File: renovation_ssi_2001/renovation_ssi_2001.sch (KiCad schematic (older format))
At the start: 72 parts, among them J1 KLPX-0848A-2-B, J2 DB15_Female, J4 Bus_ISA_8bit, J5 Pins_02x04, J6 Pins_02x03, J7 SID_Socket, Q1 PN2222A, Q2 PN2222A, U1 74LS74, U10 74LS138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

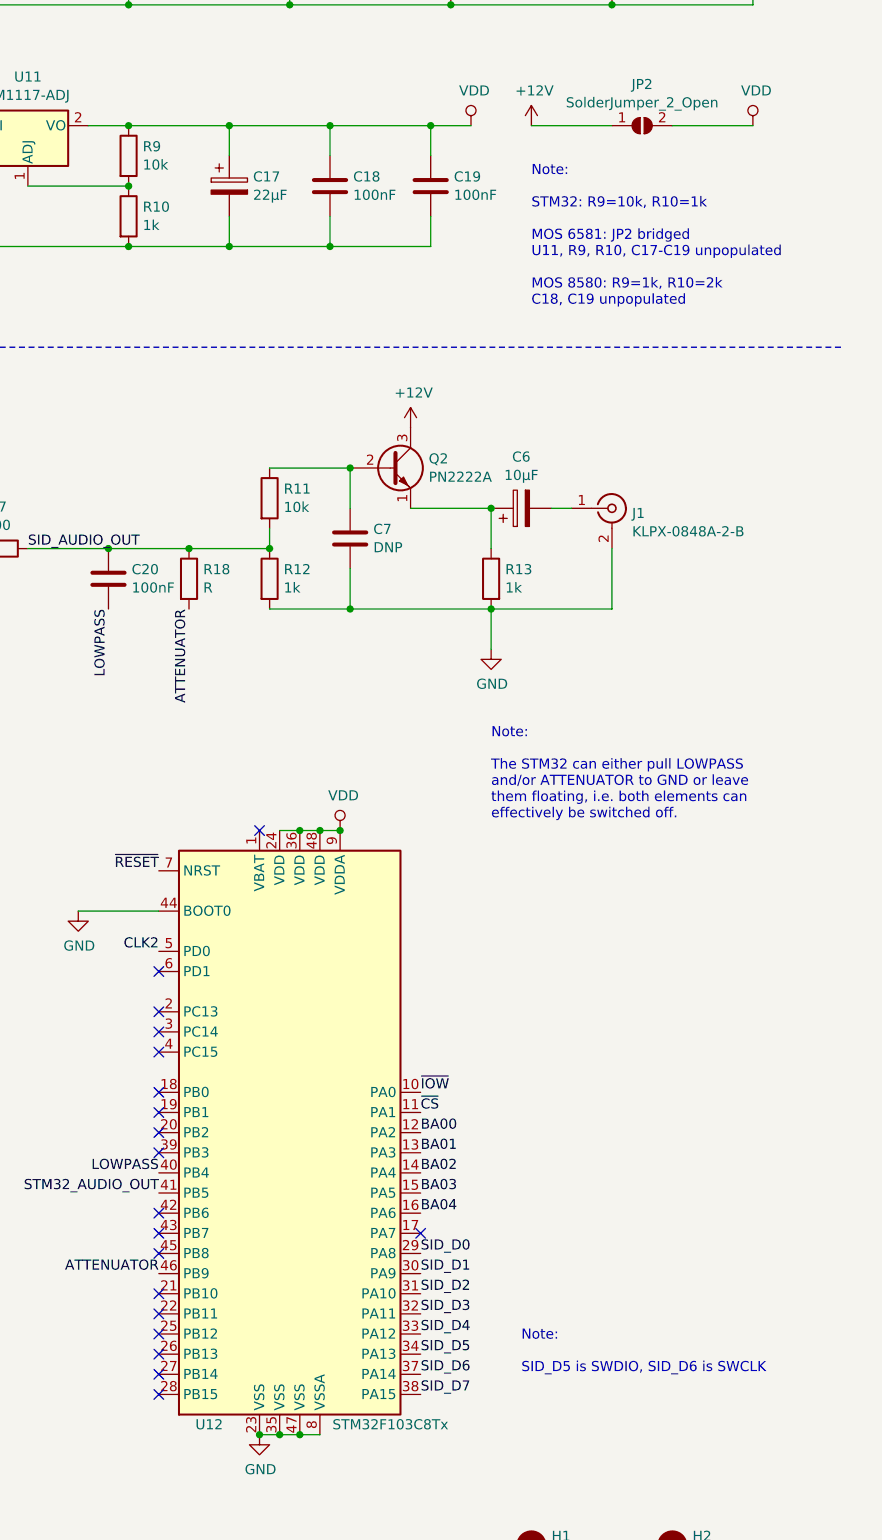
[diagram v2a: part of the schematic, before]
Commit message: correct configuration resistor values for the voltage regulator
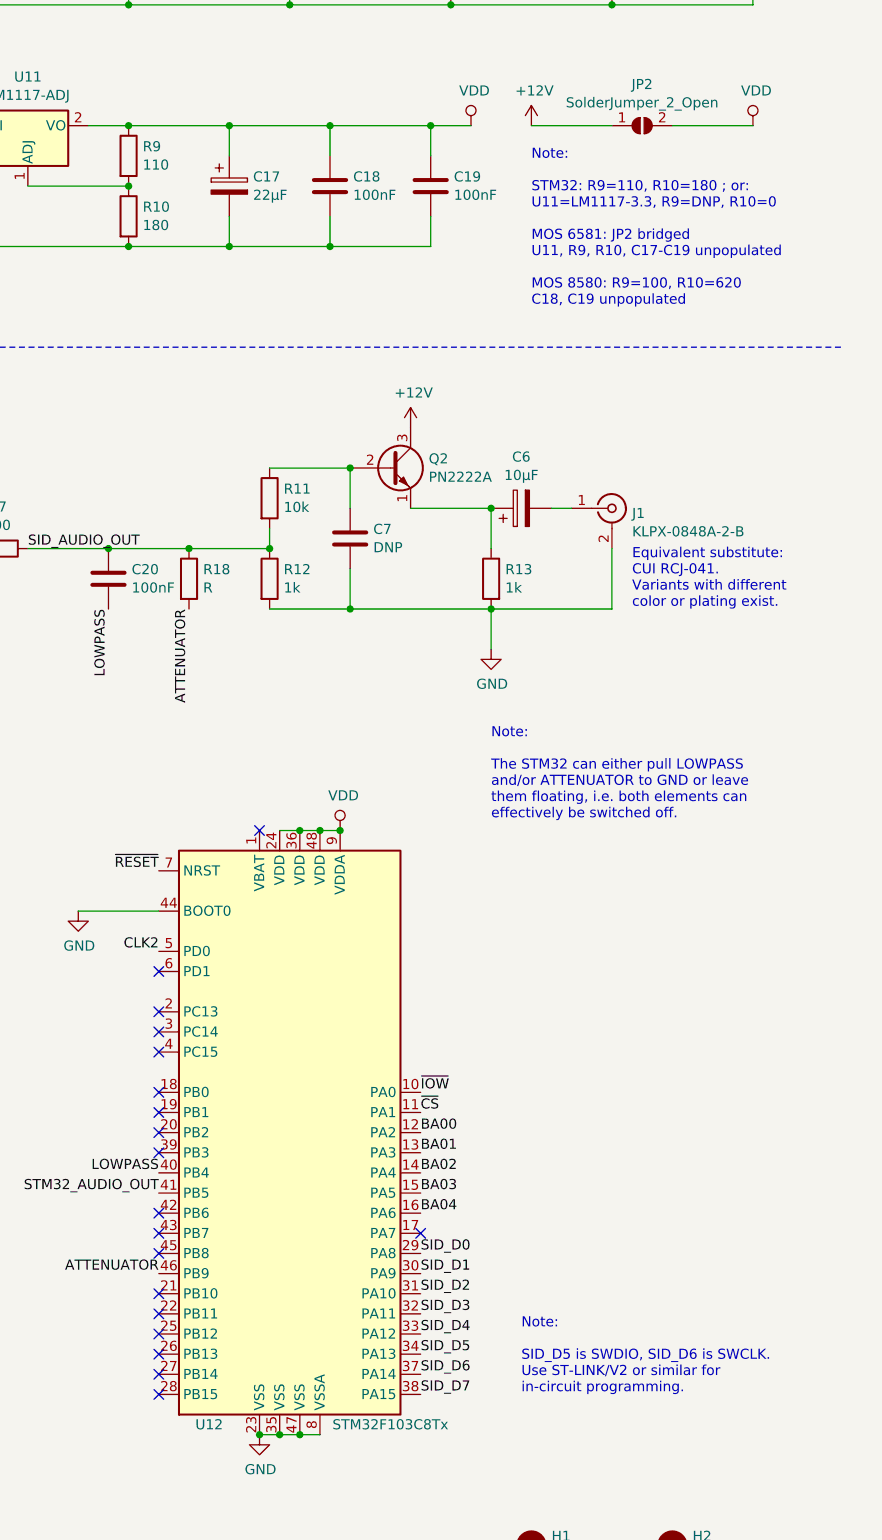
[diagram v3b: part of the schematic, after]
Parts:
- R10: value 1k -> 180
- R9: value 10k -> 110
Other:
- note added: "Equivalent substitute:\nCUI RCJ-041.\nVariants with different\ncolor or plating exist."
- note added: "Note:\n\nSID_D5 is SWDIO, SID_D6 is SWCLK.\nUse ST-LINK/V2 or similar for\nin-circuit programming."
- note added: "Note:\n\nSTM32: R9=110, R10=180 ; or:\nU11=LM1117-3.3, R9=DNP, R10=0\n\nMOS 6581: JP2 bridged\nU11, R9, R10, C17-C19 unpopulated\n\nMOS 8580: R9=100, R10=620\nC18, C19 unpopulated"
- note removed: "Note:\n\nSID_D5 is SWDIO, SID_D6 is SWCLK"
- note removed: "Note:\n\nSTM32: R9=10k, R10=1k\n\nMOS 6581: JP2 bridged\nU11, R9, R10, C17-C19 unpopulated\n\nMOS 8580: R9=1k, R10=2k\nC18, C19 unpopulated"
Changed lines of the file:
@@
 Sheet 1 1
 Title "RENOVATION SSI-2001"
-Date "2020-03-10"
+Date "2020-03-13"
 Rev ""
 Comp "Benedikt Freisen"
@@
 NoConn ~ 12650 7000
 NoConn ~ 13950 7900
-Text Notes 14450 8600 0    50   ~ 0
-Note:\n\nSID_D5 is SWDIO, SID_D6 is SWCLK
 NoConn ~ 12650 7200
 NoConn ~ 12650 7300
@@
 P 12500 2550
 F 0 "R9" H 12570 2596 50  0000 L CNN
-F 1 "10k" H 12570 2505 50  0000 L CNN
+F 1 "110" H 12570 2505 50  0000 L CNN
 F 2 "Resistor_SMD:R_0603_1608Metric" V 12430 2550 50  0001 C CNN
 F 3 "~" H 12500 2550 50  0001 C CNN
@@
 P 12500 2850
 F 0 "R10" H 12570 2896 50  0000 L CNN
-F 1 "1k" H 12570 2805 50  0000 L CNN
+F 1 "180" H 12570 2805 50  0000 L CNN
 F 2 "Resistor_SMD:R_0603_1608Metric" V 12430 2850 50  0001 C CNN
 F 3 "~" H 12500 2850 50  0001 C CNN
@@
 Wire Wire Line
 	5200 9600 5200 9700
-Text Notes 14500 3300 0    50   ~ 0
-Note:\n\nSTM32: R9=10k, R10=1k\n\nMOS 6581: JP2 bridged\nU11, R9, R10, C17-C19 unpopulated\n\nMOS 8580: R9=1k, R10=2k\nC18, C19 unpopulated
 Text Notes 9700 5700 0    50   ~ 0
 Note:\n\nSTM32: C3, C4 unpopulated\n\nMOS 6581/8580 : U12, R7, R18, C20 unpopulated\n\nJ7 is always populated and serves either\nas the socket for the SID chip or as\nprogramming port for the STM32.
@@
 Text Notes 3700 6500 0    50   ~ 0
 (Fast ISA mod: Disconnect U2 pad 4 from trace and bridge to TP1.)
+Text Notes 15000 4800 0    50   ~ 0
+Equivalent substitute:\nCUI RCJ-041.\nVariants with different\ncolor or plating exist.
+Text Notes 14500 3300 0    50   ~ 0
+Note:\n\nSTM32: R9=110, R10=180 ; or:\nU11=LM1117-3.3, R9=DNP, R10=0\n\nMOS 6581: JP2 bridged\nU11, R9, R10, C17-C19 unpopulated\n\nMOS 8580: R9=100, R10=620\nC18, C19 unpopulated
+Text Notes 14450 8700 0    50   ~ 0
+Note:\n\nSID_D5 is SWDIO, SID_D6 is SWCLK.\nUse ST-LINK/V2 or similar for\nin-circuit programming.
 $EndSCHEMATC
